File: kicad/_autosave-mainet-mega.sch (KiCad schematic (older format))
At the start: 30 parts, among them J1 Screw_Terminal_01x03, J10 Screw_Terminal_01x03, J11 Screw_Terminal_01x03, J12 Screw_Terminal_01x03, J13 Screw_Terminal_01x03, J14 Screw_Terminal_01x03, J15 Screw_Terminal_01x03, J16 Screw_Terminal_01x03, J17 Screw_Terminal_01x03, J18 Screw_Terminal_01x03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

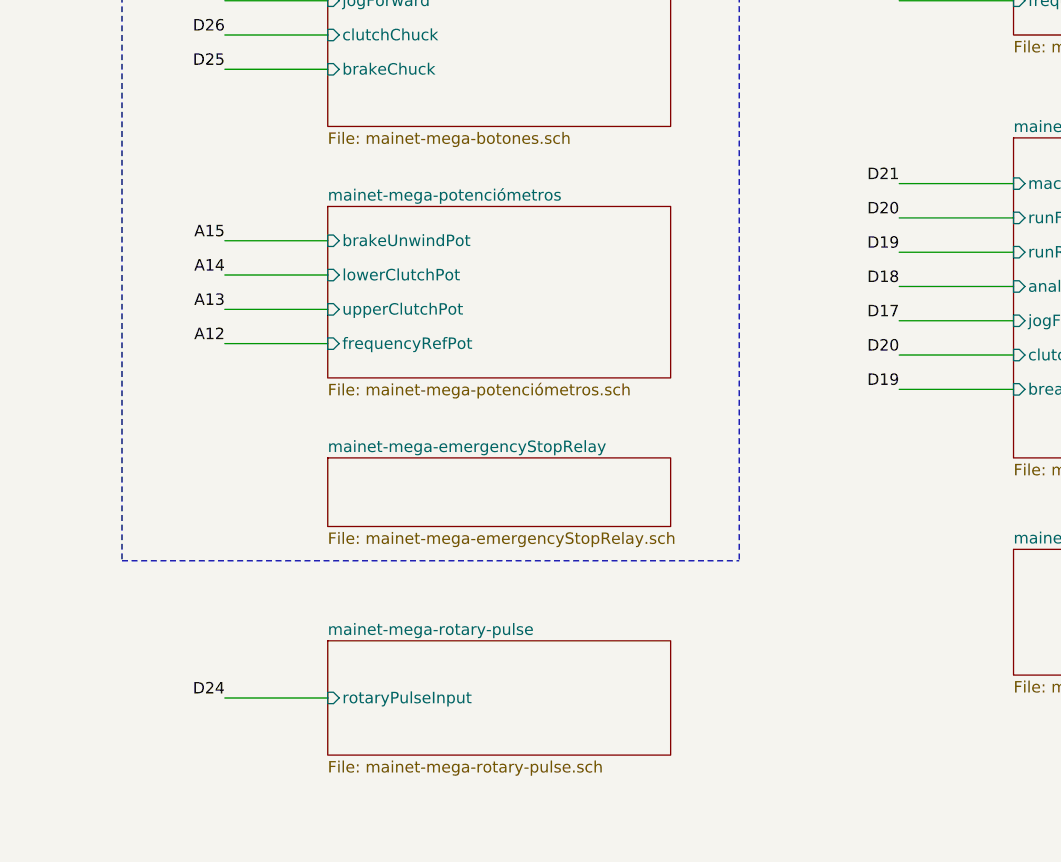
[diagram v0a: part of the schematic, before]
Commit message: Kicad: Modificaciones menores esquemáticos
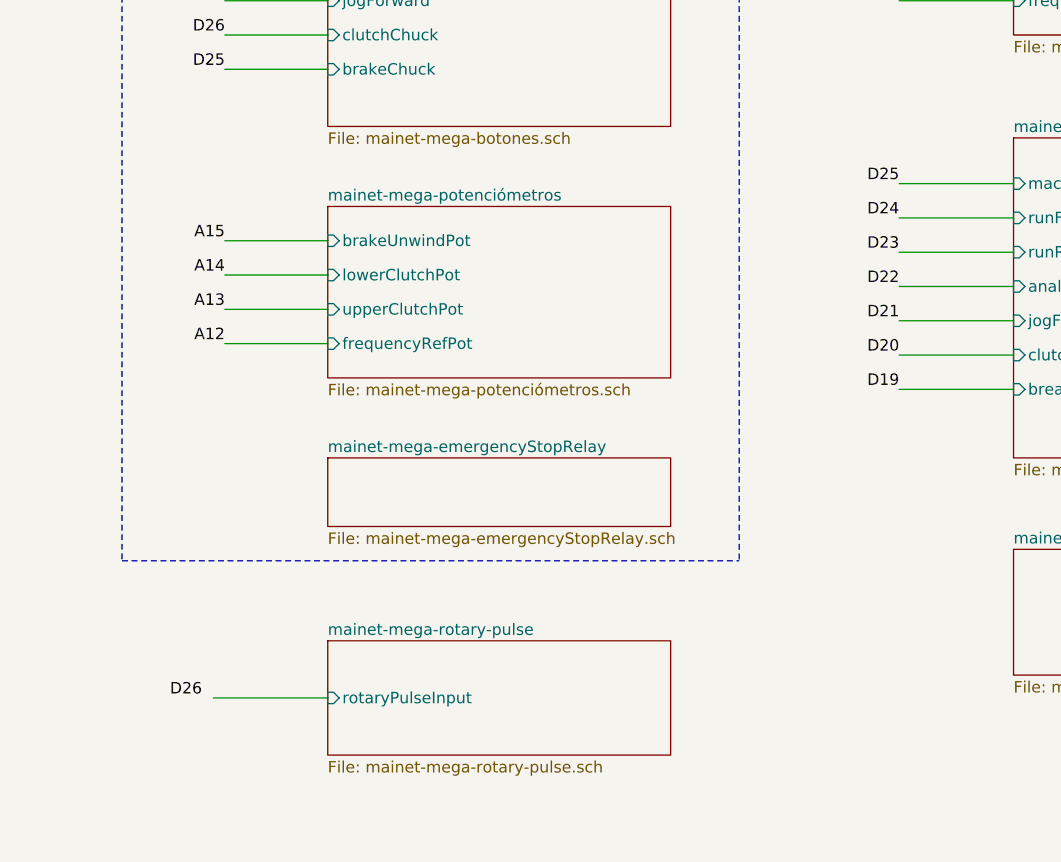
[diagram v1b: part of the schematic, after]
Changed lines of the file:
@@
 F2 "rotaryPulseInput" I L 6100 4550 50
 $EndSheet
-Text Label 5650 4550 2    50   ~ 0
-D24
+Text Label 5550 4550 2    50   ~ 0
+D26
 Text Notes 1250 1200 0    50   ~ 0
 +\n12V\n-\n
@@
 Text Notes 10600 7650 0    50   ~ 0
 27/01/2021
+Wire Wire Line
+	5600 4550 6100 4550
 $Sheet
 S 6100 900  1500 1150
@@
 	7900 600  7900 3950
 Text Label 8600 2900 2    50   ~ 0
-D17
+D21
 Wire Wire Line
 	8600 2900 9100 2900
@@
 	8600 2300 9100 2300
 Text Label 8600 2750 2    50   ~ 0
-D18
+D22
 Text Label 8600 2600 2    50   ~ 0
-D19
+D23
 Text Label 8600 2450 2    50   ~ 0
-D20
+D24
 Text Label 8600 2300 2    50   ~ 0
-D21
+D25
 $Sheet
 S 9100 2100 1500 1400
@@
 Wire Wire Line
 	5650 1800 6100 1800
-Wire Wire Line
-	5650 4550 6100 4550
 $EndSCHEMATC
